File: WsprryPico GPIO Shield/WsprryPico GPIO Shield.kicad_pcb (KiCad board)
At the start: 2 copper layers, 53.3 x 22.9 mm, 22 parts, among them J51 SMA_Adafruit_1865, Q41 BS170, U21 TPS22918DBVR

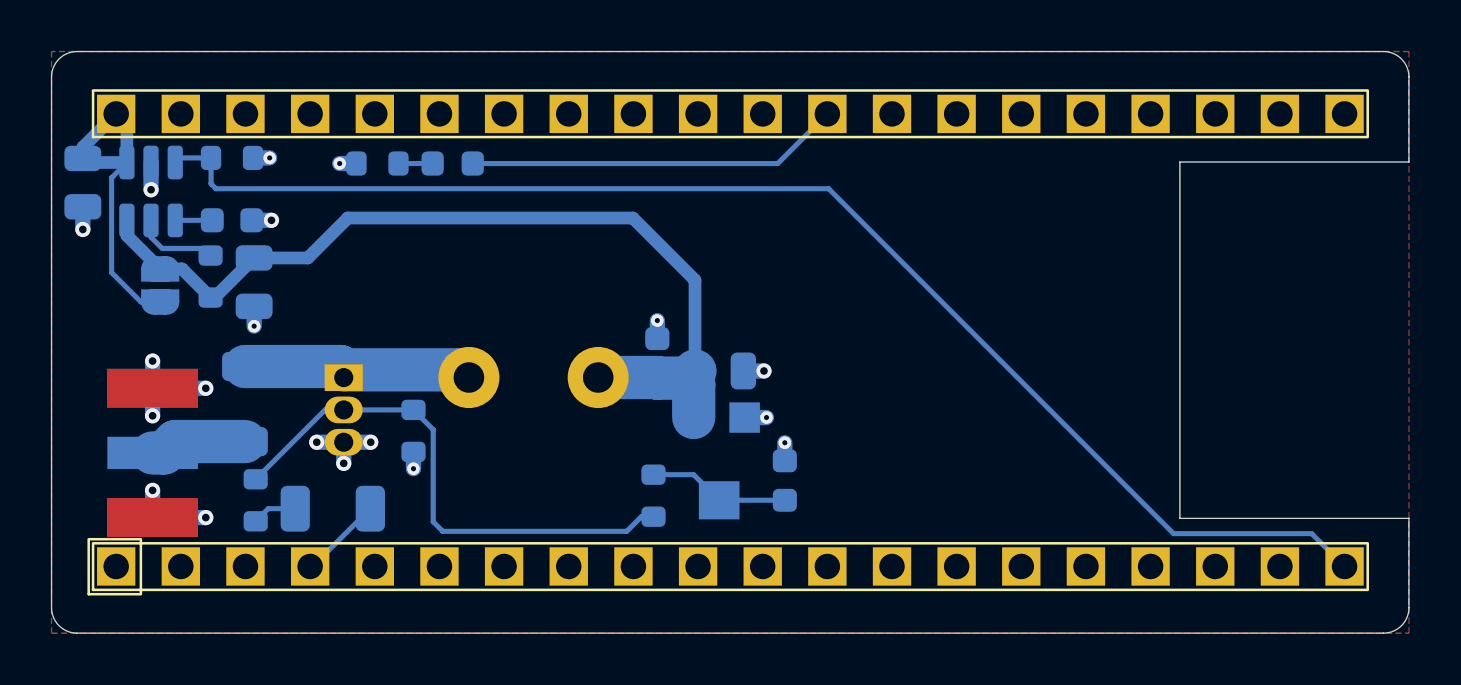
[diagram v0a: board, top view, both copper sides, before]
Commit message: Flip Pico shield assemblies and center USB reference markings
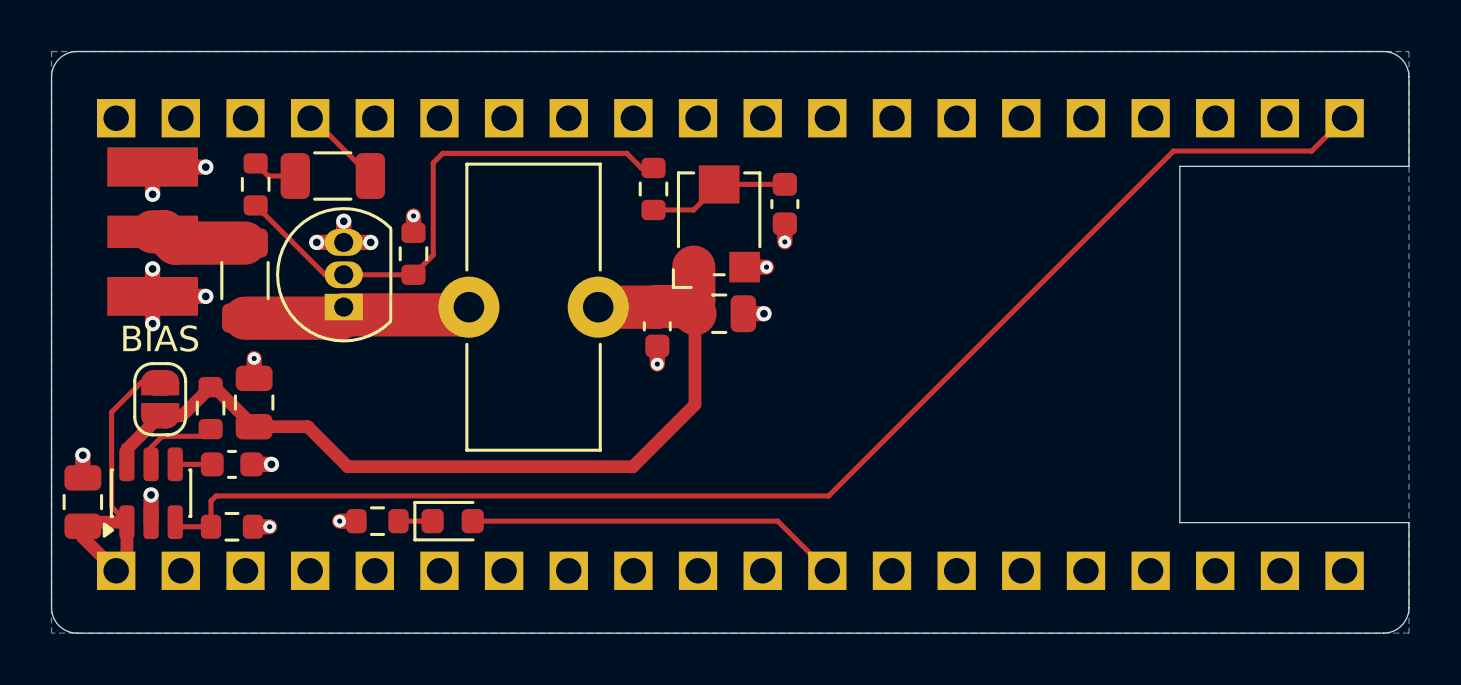
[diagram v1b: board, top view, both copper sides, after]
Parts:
- C21, C22, C23, C31, C32, C41, C42, C51, D11, J51, JP1, L41, Q41, R11, R21, R22, R31, R32, R33, RV31, U21: moved to F.Cu
- U11: moved to B.Cu
- moved R21 14.5 mm to (127.2, 97.0)
- moved D11 14.0 mm to (135.9, 96.8)
- moved R11 14.0 mm to (132.9, 96.8)
- moved C31 13.1 mm to (131.2, 83.2)
- moved C21 12.5 mm to (121.4, 96.0), turned to 90 degrees
- moved R31 12.4 mm to (128.2, 83.6), turned to -90 degrees
- moved R32 12.0 mm to (143.8, 83.8), turned to 90 degrees
- moved U21 11.9 mm to (124.0, 95.7), turned to 90 degrees
- moved C32 10.9 mm to (148.9, 84.3), turned to 90 degrees
- moved C22 9.59 mm to (127.2, 94.6)
- moved RV31 9.51 mm to (146.4, 85.0), turned to 90 degrees
- moved J51 8.69 mm to (121.8, 85.4), turned to -90 degrees
- moved R33 6.96 mm to (134.3, 86.3), turned to -90 degrees
- moved R22 5.17 mm to (126.4, 92.4), turned to -90 degrees
- moved C51 4.85 mm to (127.7, 87.3), turned to 90 degrees
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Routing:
- added copper zone on B.Cu, net GND
- removed copper zone on F.Cu, net GND
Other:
- outline, holes or cut-outs redrawn
